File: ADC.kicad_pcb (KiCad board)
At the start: 4 copper layers, 242.5 x 165 mm, 188 parts, among them J1 RCA, J2 RCA, J3 IEC-C13-SOCKET, P1 CONN_6, P10 CONN_2, P11 CONN_2, P12 CONN_2, P13 CONN_4, P14 CONN_2, P15 CONN_2, P16 CONN_2, P17 CONN_4, P18 CONN_1, P19 CONN_1, P2 CONN_6, P20 CONN_1, P21 CONN_1, P22 CONN_1, P3 CONN_6, P4 CONN_6, P5 CONN_1, P6 CONN_2, P7 CONN_2, P8 CONN_2, P9 CONN_2, Q1 BD241A, Q2 BD241A, Q3 BD242, T1 TRIAD-FS20-300-C2, T2 TRIAD-FS48-750-C2, U1 OPA27, U10 P0300ECL, U11 P0300ECL, U12 MC7805C, U13 LM7818CT, U14 LM7918CT, U15 LME49740, U16 LME49740, U2 OPA27, U3 OPA27, U4 2N6507, U5 2N6507, U6 2N6507, U7 REF02, U8 2N6507, U9 OPA27

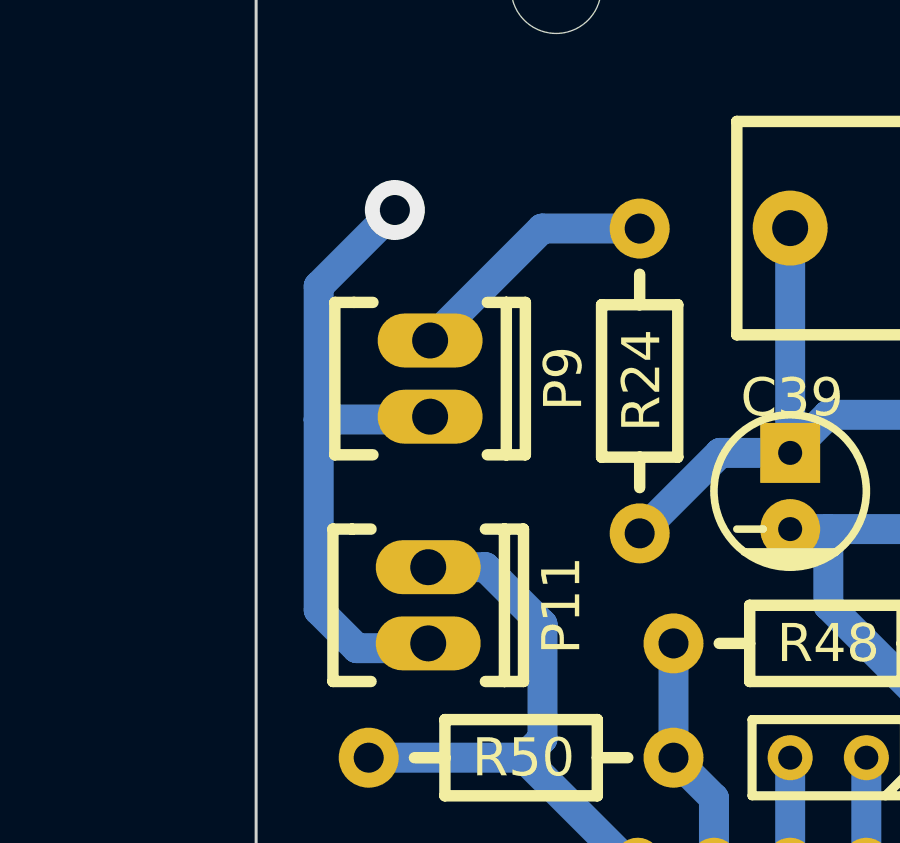
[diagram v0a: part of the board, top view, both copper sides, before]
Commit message: Minor ground rerouting.
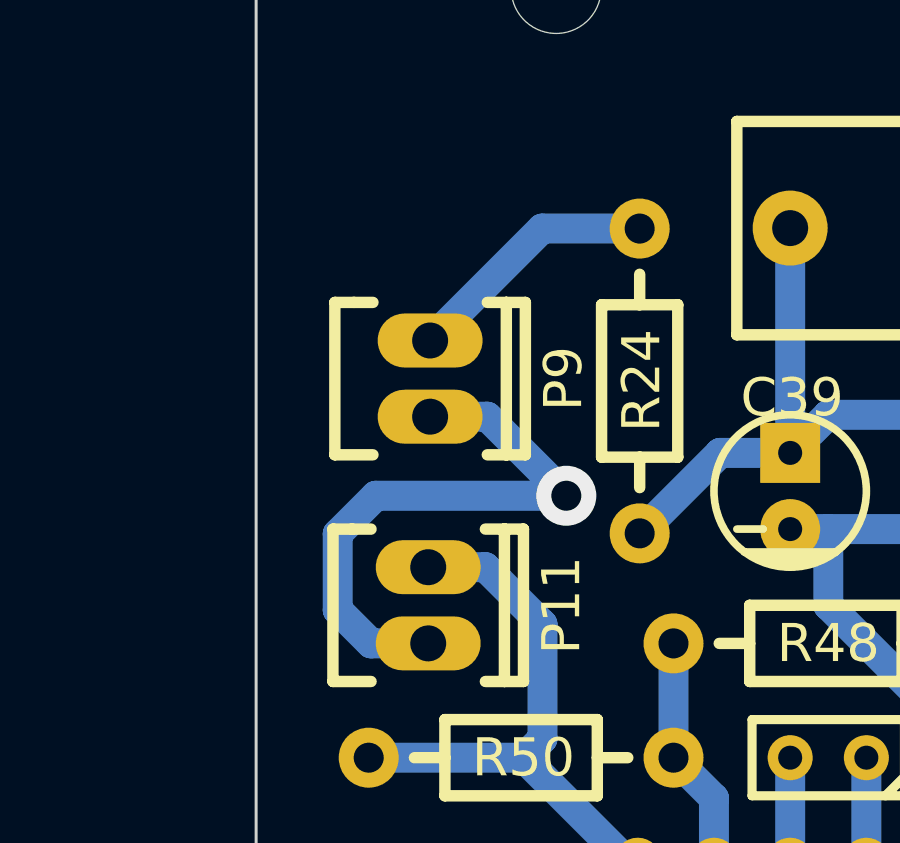
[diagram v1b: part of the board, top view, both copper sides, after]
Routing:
- net /Clipper/AGND: track 342.5 -> 340.3 mm
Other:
- net class Power: trace_width 2 -> 1

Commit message: Moved component designators on silkscreen so that they are not covered by components. Combined silkscreen and user top layers into a cover layer for printing.
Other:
- board text added: "+4/-15/AGND/+15"
- board text added: "+5/DGND"
- board text added: "+5/DGND/SAFGND/ +18/AGND/-18"
- board text added: "-18/AGND/18/SAFGND/DGND/+5"
- board text added: "LIN/G"
- board text added: "LOUT/GND"
- board text added: "RIN/G"
- board text added: "ROUT/GND"
- board text added: "SAFETY GND"
